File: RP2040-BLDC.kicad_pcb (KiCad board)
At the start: 4 copper layers, 40.2 x 35.8 mm, 33 parts, among them J1 Motor, J2 Conn_01x02, J3 USB_B_Micro, J4 Motor power, U2 AS5048A, U6 RP2040

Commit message: WIP
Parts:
- removed H1, H2, H3, H4: MountingHole, MountingHole:MountingHole_3.2mm_M3
- added C18: 4.7u, Capacitor_SMD:C_0805_2012Metric, F.Cu at (58.4, 45.0)
- added C19: 0.1u, Capacitor_SMD:C_0402_1005Metric, F.Cu at (54.8, 43.4)
- added C20: 0.1u, Capacitor_SMD:C_0402_1005Metric, F.Cu at (54.8, 45.4)
- added C21: 22u, Capacitor_SMD:CP_Elec_5x5.4, F.Cu at (80.6, 38.5)
- added C22: 22u, Capacitor_SMD:CP_Elec_5x5.4, F.Cu at (80.2, 45.0)
- added C23: 0.1u, Capacitor_SMD:C_0402_1005Metric, F.Cu at (61.8, 96.7)
- added C24: 0.1u, Capacitor_SMD:C_0402_1005Metric, F.Cu at (60.2, 98.9)
- added C25: 4.7u, Capacitor_SMD:C_0805_2012Metric, F.Cu at (69.5, 98.4)
- added C26: 0.1u, Capacitor_SMD:C_0402_1005Metric, F.Cu at (63.5, 102.0)
- added C27: 0.1u, Capacitor_SMD:C_0402_1005Metric, F.Cu at (62.1, 99.7)
- added C28: 22u, Capacitor_SMD:CP_Elec_5x5.4, F.Cu at (58.2, 104.2)
- added C29: 22u, Capacitor_SMD:CP_Elec_5x5.4, F.Cu at (80.0, 96.8)
- added C3: 0.1u, Capacitor_SMD:C_0402_1005Metric, F.Cu at (54.8, 39.5)
- added C5: 0.1u, Capacitor_SMD:C_0402_1005Metric, F.Cu at (54.8, 41.5)
- added D2: MBR1020VL, Diode_SMD:D_SOD-123F, F.Cu at (79.0, 59.1)
- added J5: AS5048A, Connector_JST:JST_SH_BM05B-SRSS-TB_1x05-1MP_P1.00mm_Vertical, F.Cu at (88.1, 51.3)
- added J6: M1, Connector_JST:JST_XH_S3B-XH-A_1x03_P2.50mm_Horizontal, F.Cu at (69.9, 45.0)
- added J7: M2, Connector_JST:JST_XH_S3B-XH-A_1x03_P2.50mm_Horizontal, F.Cu at (64.8, 106.4)
- added J8: AS5048A, Connector_JST:JST_SH_BM05B-SRSS-TB_1x05-1MP_P1.00mm_Vertical, F.Cu at (66.0, 91.8)
- added R6: 5.1k, Resistor_SMD:R_0402_1005Metric, F.Cu at (63.1, 52.1)
- added R7: 5.1k, Resistor_SMD:R_0402_1005Metric, F.Cu at (59.0, 94.2)
- J1: value Motor -> MPWR; footprint Connector_JST:JST_XH_B3B-XH-A_1x03_P2.50mm_Vertical -> Connector_PinHeader_2.54mm:PinHeader_1x02_P2.54mm_Vertical
- J4: value Motor power -> I2C5V; footprint Connector_JST:JST_XH_B2B-XH-A_1x02_P2.50mm_Vertical -> Connector_JST:JST_SH_BM04B-SRSS-TB_1x04-1MP_P1.00mm_Vertical
- U2: value AS5048A -> ~; footprint Package_SO:TSSOP-14_4.4x5mm_P0.65mm -> MyLibrary:WQFN-24_EP_2.93x2.93_Pitch0.4mm; moved to F.Cu
- moved J3 57.5 mm to (86.1, 74.6), turned to 90 degrees
- moved R2 54.6 mm to (80.2, 66.6), turned to 90 degrees
- moved C4 53.6 mm to (80.2, 69.0), turned to -90 degrees
- moved D1 51.9 mm to (81.4, 83.9), turned to 0 degrees
- moved U1 50.3 mm to (77.3, 67.3), turned to -90 degrees
- moved C17 49.2 mm to (77.8, 72.4), turned to 0 degrees
- moved C6 49.2 mm to (77.6, 71.4), turned to 0 degrees
- moved R1 48.9 mm to (75.3, 64.9), turned to -90 degrees
- moved C9 48.4 mm to (77.4, 73.5), turned to 0 degrees
- moved R4 47.4 mm to (76.8, 74.5), turned to 180 degrees
- moved R5 47.2 mm to (76.8, 75.5), turned to 180 degrees
- moved C8 46.9 mm to (76.7, 76.5), turned to 0 degrees
- moved C10 46.9 mm to (76.7, 77.5), turned to 0 degrees
- moved J2 45.8 mm to (72.9, 64.9), turned to -90 degrees
- moved C11 45.3 mm to (73.8, 68.1), turned to 90 degrees
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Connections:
- D1 pad 1: VCOM -> +5V
- J1 pad 1: /M1 -> GND
- J1 pad 2: /M2 -> +BATT
- J4 pad 1: GND -> /I2C0_SCL
- J4 pad 2: Vdrive -> /I2C0_SDA
- U2 pad 1: unconnected-(U2-~{CSn}-Pad1) -> /Driver sensor pair/DRV~{FAULT}
- U2 pad 10: unconnected-(U2-TEST-Pad10) -> /Driver sensor pair/MA
- U2 pad 11: unconnected-(U2-VDD5V-Pad11) -> /Driver sensor pair/MB
- U2 pad 12: unconnected-(U2-VDD3V-Pad12) -> /Driver sensor pair/MC
- U2 pad 2: unconnected-(U2-CLK-Pad2) -> Net-(U2-CSAREF)
- U2 pad 3: unconnected-(U2-MISO-Pad3) -> /Driver sensor pair/SOC
- U2 pad 4: unconnected-(U2-MOSI-Pad4) -> /Driver sensor pair/SOB
- U2 pad 5: unconnected-(U2-TEST-Pad5) -> /Driver sensor pair/SOA
- U2 pad 6: unconnected-(U2-TEST-Pad6) -> Net-(U2-CP)
- U2 pad 7: unconnected-(U2-TEST-Pad7) -> +5V
- U2 pad 8: unconnected-(U2-TEST-Pad8) -> +BATT
- U2 pad 9: unconnected-(U2-TEST-Pad9) -> GND
- U3 pad 1: unconnected-(U3-~{FAULT}-Pad1) -> /Driver sensor pair1/DRV~{FAULT}
- U3 pad 10: /M1 -> /Driver sensor pair1/MA
- U3 pad 11: /M2 -> /Driver sensor pair1/MB
- U3 pad 12: /M3 -> /Driver sensor pair1/MC
- U3 pad 17: unconnected-(U3-AVDD-Pad17) -> /Driver sensor pair1/3.3VOUT
- U3 pad 19: unconnected-(U3-PWM_SYNC-Pad19) -> /Driver sensor pair1/PWM_SYNC
- U3 pad 2: unconnected-(U3-CSAREF-Pad2) -> Net-(U3-CSAREF)
- U3 pad 20: /DRV_CSn -> /Driver sensor pair1/DRV~{CS}
- U3 pad 21: /SPI0_RX -> /Driver sensor pair1/SDO
- U3 pad 22: /SPI0_TX -> /Driver sensor pair1/SDI
- U3 pad 23: /SPI0_SCK -> /Driver sensor pair1/SPI_CLK
- U3 pad 24: unconnected-(U3-~{SLEEP}-Pad24) -> /Driver sensor pair1/~{SLEEP}
- U3 pad 25: (no net) -> GND
- U3 pad 3: unconnected-(U3-SOC-Pad3) -> /Driver sensor pair1/SOC
- U3 pad 4: unconnected-(U3-SOB-Pad4) -> /Driver sensor pair1/SOB
- U3 pad 5: unconnected-(U3-SOA-Pad5) -> /Driver sensor pair1/SOA
- U3 pad 6: unconnected-(U3-CP-Pad6) -> Net-(U3-CP)
- U3 pad 7: VCOM -> +5V
- U3 pad 8: Vdrive -> +BATT
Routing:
- net +5V: track 0.00 -> 36.9 mm, vias 0 -> 4
- net +3V3: track 19.9 -> 0.00 mm
- net /QSPI_SS: track 12.8 -> 0.00 mm
- net /USB_D+: track 10.5 -> 0.00 mm
- net /USB_D-: track 10.5 -> 0.00 mm
- net /Driver sensor pair1/SPI_CLK: track 0.00 -> 10.2 mm
- net /QSPI_SD1: track 9.04 -> 0.00 mm
- net /QSPI_SD2: track 7.64 -> 0.00 mm
- net +1V1: track 7.51 -> 0.00 mm
- net /QSPI_SD3: track 6.37 -> 0.00 mm
- net /QSPI_SCLK: track 5.75 -> 0.00 mm
- net /QSPI_SD0: track 5.13 -> 0.00 mm
- net /M1: track 4.74 -> 0.00 mm
- net /M3: track 4.23 -> 0.00 mm
- net Net-(U3-CP): track 0.00 -> 4.05 mm
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- added copper zone on F.Cu, net +5V
- added copper zone on F.Cu, net +BATT
- added copper zone on F.Cu, net /Driver sensor pair1/MA
- added copper zone on F.Cu, net /Driver sensor pair1/MB
- added copper zone on F.Cu, net /Driver sensor pair1/MC
- added copper zone on F.Cu, net GND
- added copper zone on In1.Cu, net GND
- added copper zone on In2.Cu, net GND
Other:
- board size 40.2 x 35.8 mm -> 41.4 x 81.2 mm

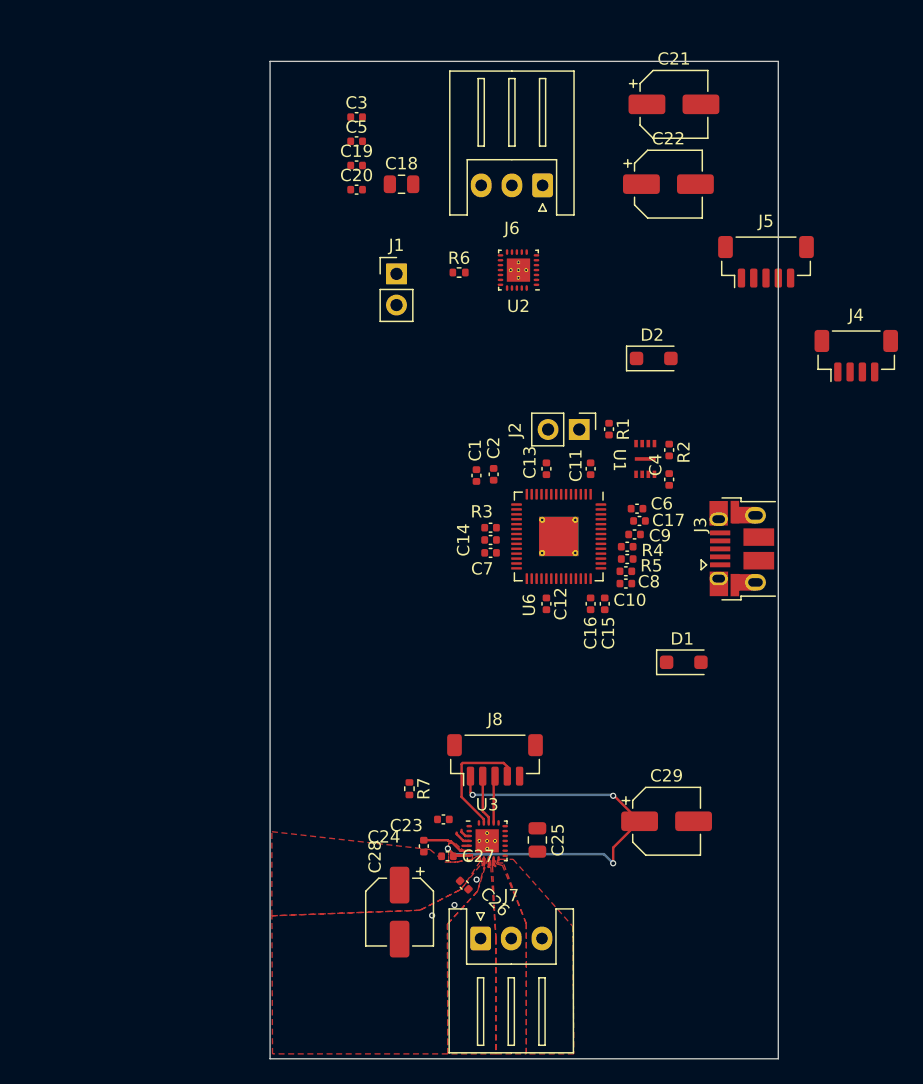
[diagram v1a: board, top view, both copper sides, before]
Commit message: First pass at routing board.
- Add INA219 current sensor and shunt
- Route motor traces.
- Still need to fix a few footprints.
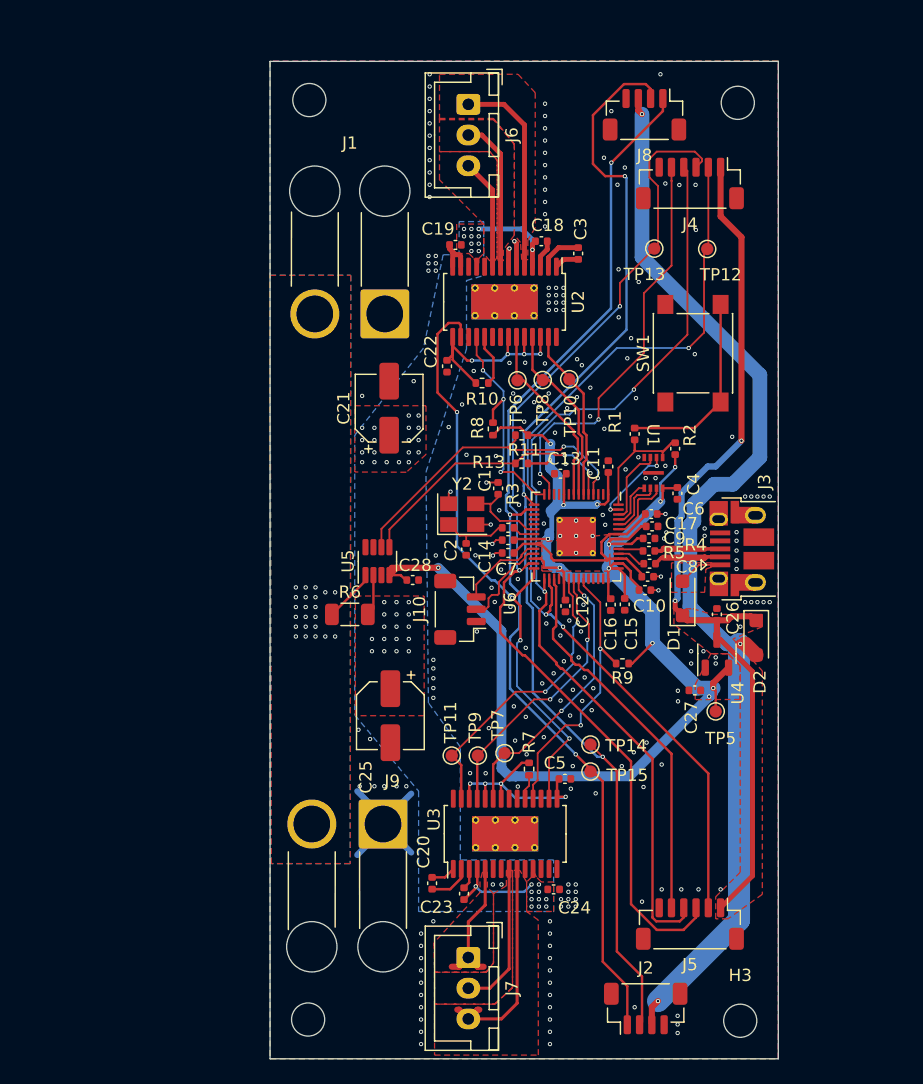
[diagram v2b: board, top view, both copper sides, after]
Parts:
- removed C29: 22u, Capacitor_SMD:CP_Elec_5x5.4
- added H1: MountingHole, MountingHole:MountingHole_2.7mm_M2.5, F.Cu at (50.9, 38.1)
- added H2: MountingHole, MountingHole:MountingHole_2.7mm_M2.5, F.Cu at (85.8, 38.3)
- added H3: MountingHole, MountingHole:MountingHole_2.7mm_M2.5, F.Cu at (86.0, 113.1)
- added H4: MountingHole, MountingHole:MountingHole_2.7mm_M2.5, F.Cu at (50.8, 113.0)
- added J10: DBG, Connector_JST:JST_SH_BM03B-SRSS-TB_1x03-1MP_P1.00mm_Vertical, F.Cu at (63.2, 79.6)
- added J9: MPWR, MyLibrary:SolderWire-2.5sqmm_1x02_P7.2mm_D2.4mm_OD3.6mm_ShortRelief, F.Cu at (56.9, 97.1)
- added R10: 10k, Resistor_SMD:R_0402_1005Metric, F.Cu at (65.0, 61.1)
- added R11: 2k, Resistor_SMD:R_0402_1005Metric, F.Cu at (68.2, 65.4)
- added R13: 2k, Resistor_SMD:R_0402_1005Metric, F.Cu at (68.2, 67.7)
- added R8: 10k, Resistor_SMD:R_0402_1005Metric, F.Cu at (65.9, 64.9)
- added R9: 10k, Resistor_SMD:R_0402_1005Metric, F.Cu at (76.4, 84.0)
- added SW1: Flash, Button_Switch_SMD:SW_Push_1P1T_NO_6x6mm_H9.5mm, F.Cu at (82.2, 58.7)
- added TP10: TestPoint_Small, TestPoint:TestPoint_Pad_D1.0mm, F.Cu at (72.1, 60.8)
- added TP11: TestPoint_Small, TestPoint:TestPoint_Pad_D1.0mm, F.Cu at (62.5, 91.5)
- added TP12: TestPoint_Small, TestPoint:TestPoint_Pad_D1.0mm, F.Cu at (83.3, 50.2)
- added TP13: TestPoint_Small, TestPoint:TestPoint_Pad_D1.0mm, F.Cu at (79.0, 50.2)
- added TP14: TestPoint_Small, TestPoint:TestPoint_Pad_D1.0mm, F.Cu at (73.8, 90.6)
- added TP15: TestPoint_Small, TestPoint:TestPoint_Pad_D1.0mm, F.Cu at (73.8, 92.8)
- added TP5: TestPoint_Small, TestPoint:TestPoint_Pad_D1.0mm, F.Cu at (84.0, 87.9)
- added TP6: TestPoint_Small, TestPoint:TestPoint_Pad_D1.0mm, F.Cu at (67.8, 60.9)
- added TP7: TestPoint_Small, TestPoint:TestPoint_Pad_D1.0mm, F.Cu at (66.8, 91.3)
- added TP8: TestPoint_Small, TestPoint:TestPoint_Pad_D1.0mm, F.Cu at (69.9, 60.9)
- added TP9: TestPoint_Small, TestPoint:TestPoint_Pad_D1.0mm, F.Cu at (64.6, 91.5)
- added U4: XC6206PxxxMR, Package_TO_SOT_SMD:SOT-23-3, F.Cu at (84.1, 83.2)
- added U5: INA219AxDCN, Package_TO_SOT_SMD:SOT-23-8, F.Cu at (56.4, 75.7)
- added Y2: 12MHz X322512MSB4SI, Crystal:Crystal_SMD_3225-4Pin_3.2x2.5mm, F.Cu at (63.4, 71.8)
- C18: value 4.7u -> 0.1u; footprint Capacitor_SMD:C_0805_2012Metric -> Capacitor_SMD:C_0402_1005Metric
- C20, C3: value 0.1u -> 0.01u
- C21: value 22u -> 100u
- C22: value 22u -> 0.47u; footprint Capacitor_SMD:CP_Elec_5x5.4 -> Capacitor_SMD:C_0402_1005Metric
- C25: value 4.7u -> 100u; footprint Capacitor_SMD:C_0805_2012Metric -> Capacitor_SMD:CP_Elec_5x5.4
- C26, C27: value 0.1u -> 1u
- C28: value 22u -> C_Small; footprint Capacitor_SMD:CP_Elec_5x5.4 -> Capacitor_SMD:C_0402_1005Metric
- C5: value 0.1u -> 0.47u
- J1: footprint Connector_PinHeader_2.54mm:PinHeader_1x02_P2.54mm_Vertical -> MyLibrary:SolderWire-2.5sqmm_1x02_P7.2mm_D2.4mm_OD3.6mm_ShortRelief_Flipped
- J2: value Conn_01x02 -> Conn_01x04_MountingPin; footprint Connector_PinHeader_2.54mm:PinHeader_1x02_P2.54mm_Vertical -> Connector_JST:JST_SH_BM04B-SRSS-TB_1x04-1MP_P1.00mm_Vertical
- J4: value I2C5V -> Conn_01x06_MountingPin; footprint Connector_JST:JST_SH_BM04B-SRSS-TB_1x04-1MP_P1.00mm_Vertical -> Connector_JST:JST_SH_BM06B-SRSS-TB_1x06-1MP_P1.00mm_Vertical
- J5: value AS5048A -> Conn_01x06_MountingPin; footprint Connector_JST:JST_SH_BM05B-SRSS-TB_1x05-1MP_P1.00mm_Vertical -> Connector_JST:JST_SH_BM06B-SRSS-TB_1x06-1MP_P1.00mm_Vertical
- J6, J7: footprint Connector_JST:JST_XH_S3B-XH-A_1x03_P2.50mm_Horizontal -> Connector_JST:JST_XH_B3B-XH-A_1x03_P2.50mm_Vertical
- J8: value AS5048A -> Conn_01x04_MountingPin; footprint Connector_JST:JST_SH_BM05B-SRSS-TB_1x05-1MP_P1.00mm_Vertical -> Connector_JST:JST_SH_BM04B-SRSS-TB_1x04-1MP_P1.00mm_Vertical
- R6: value 5.1k -> 0.01; footprint Resistor_SMD:R_0402_1005Metric -> Resistor_SMD:R_1206_3216Metric
- R7: value 5.1k -> 10k
- U2, U3: value ~ -> DRV8313; footprint MyLibrary:WQFN-24_EP_2.93x2.93_Pitch0.4mm -> Package_SO:HTSSOP-28-1EP_4.4x9.7mm_P0.65mm_EP2.85x5.4mm_ThermalVias
- moved C20 56.8 mm to (60.9, 101.9), turned to -90 degrees
- moved C5 54.6 mm to (71.7, 93.4)
- moved J5 54.3 mm to (81.9, 105.2), turned to 180 degrees
- moved J8 53.9 mm to (78.2, 39.3), turned to 180 degrees
- moved J2 47.5 mm to (78.3, 112.1), turned to 0 degrees
- moved C21 33.9 mm to (57.4, 63.2), turned to 90 degrees
- moved C26 30.2 mm to (84.1, 80.0), turned to 90 degrees
- moved R6 29.2 mm to (54.2, 80.0)
- moved C28 27.1 mm to (59.3, 77.2), turned to 0 degrees
- moved C27 24.3 mm to (82.3, 86.2)
- moved D2 24.2 mm to (87.3, 81.9), turned to -90 degrees
- moved C22 23.4 mm to (62.1, 59.8), turned to -90 degrees
- moved C3 21.2 mm to (72.8, 50.6), turned to 90 degrees
- moved J4 19.5 mm to (81.9, 44.9), turned to 180 degrees
- moved C25 15.7 mm to (57.5, 88.2)
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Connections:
- C18 pad 1: +3.3V -> +BATT
- C18 pad 2: GND -> Net-(U2-VCP)
- C20 pad 1: +5V -> Net-(U3-CPL)
- C20 pad 2: GND -> Net-(U3-CPH)
- C22 pad 1: +5V -> /Driver sensor pair/DRV3.3VOUT
- C23 pad 1: Net-(U3-CSAREF) -> +BATT
- C23 pad 2: GND -> Net-(U3-VCP)
- C24 pad 2: Net-(U3-CP) -> GND
- C25 pad 1: /Driver sensor pair1/3.3VOUT -> +BATT
- C26 pad 1: +BATT -> +5V
- C27 pad 1: +5V -> +3V3
- C28 pad 1: +BATT -> +3V3
- C3 pad 1: Net-(U2-CSAREF) -> Net-(U2-CPL)
- C3 pad 2: GND -> Net-(U2-CPH)
- C5 pad 1: +BATT -> /Driver sensor pair1/DRV3.3VOUT
- C5 pad 2: Net-(U2-CP) -> GND
- J1 pad 2: +BATT -> Net-(J1-Pin_2)
- J2 pad 1: /~{USB_BOOT} -> /I2C0_SCL
- J2 pad 2: GND -> /I2C0_SDA
- J4 pad 1: /I2C0_SCL -> +5V
- J4 pad 2: /I2C0_SDA -> /SPI0_TX
- J4 pad 3: Net-(D2-A) -> /SPI0_RX
- J4 pad 4: GND -> /SPI0_SCK
- J4 pad MP: (no net) -> GND
- J5 pad 2: /Driver sensor pair/SDI -> /SPI0_TX
- J5 pad 3: /Driver sensor pair/SDO -> /SPI0_RX
- J5 pad 4: /Driver sensor pair/SPI_CLK -> /SPI0_SCK
- J5 pad 5: /Driver sensor pair/SEN~{CS} -> /SEN2CS
- J5 pad MP: (no net) -> GND
- J8 pad 1: +5V -> /I2C0_SCL
- J8 pad 2: /Driver sensor pair1/SDI -> /I2C0_SDA
- J8 pad 3: /Driver sensor pair1/SDO -> Net-(D2-A)
- J8 pad 4: /Driver sensor pair1/SPI_CLK -> GND
- J8 pad MP: (no net) -> GND
- R6 pad 1: +3.3V -> Net-(J1-Pin_2)
- R6 pad 2: /Driver sensor pair/DRV~{FAULT} -> +BATT
- R7 pad 1: /Driver sensor pair1/3.3VOUT -> Net-(U3-~{COMPO})
- R7 pad 2: /Driver sensor pair1/DRV~{FAULT} -> /Driver sensor pair1/DRV3.3VOUT
- U2 pad 1: /Driver sensor pair/DRV~{FAULT} -> Net-(U2-CPL)
- U2 pad 10: /Driver sensor pair/MA -> GND
- U2 pad 11: /Driver sensor pair/MB -> +BATT
- U2 pad 12: /Driver sensor pair/MC -> GND
- U2 pad 13: unconnected-(U2-NC-Pad13) -> GND
- U2 pad 14: unconnected-(U2-AD1-Pad14) -> GND
- U2 pad 15: unconnected-(U2-AD0-Pad15) -> /Driver sensor pair/DRV3.3VOUT
- U2 pad 16: GND -> /DRV~{RESET}
- U2 pad 17: +3.3V -> /Driver sensor pair/~{SLEEP}
- U2 pad 18: unconnected-(U2-NC-Pad18) -> /DRV1FAULT
- U2 pad 19: /Driver sensor pair/PWM_SYNC -> Net-(U2-~{COMPO})
- U2 pad 2: Net-(U2-CSAREF) -> Net-(U2-CPH)
- U2 pad 20: /Driver sensor pair/DRV~{CS} -> GND
- U2 pad 21: /Driver sensor pair/SDO -> unconnected-(U2-NC-Pad21)
- U2 pad 22: /Driver sensor pair/SDI -> /Driver sensor pair/DRV3.3VOUT
- U2 pad 23: /Driver sensor pair/SPI_CLK -> /DRV1IN3
- U2 pad 24: /Driver sensor pair/~{SLEEP} -> /Driver sensor pair/DRV3.3VOUT
- U2 pad 25: GND -> /DRV1IN2
- U2 pad 3: /Driver sensor pair/SOC -> Net-(U2-VCP)
- U2 pad 4: /Driver sensor pair/SOB -> +BATT
- U2 pad 5: /Driver sensor pair/SOA -> /Driver sensor pair/MA
- U2 pad 6: Net-(U2-CP) -> GND
- U2 pad 7: +5V -> GND
- U2 pad 8: +BATT -> /Driver sensor pair/MB
- U2 pad 9: GND -> /Driver sensor pair/MC
- U3 pad 1: /Driver sensor pair1/DRV~{FAULT} -> Net-(U3-CPL)
- U3 pad 10: /Driver sensor pair1/MA -> GND
- U3 pad 11: /Driver sensor pair1/MB -> +BATT
- U3 pad 12: /Driver sensor pair1/MC -> GND
- U3 pad 13: unconnected-(U3-NC-Pad13) -> GND
- U3 pad 14: unconnected-(U3-AD1-Pad14) -> GND
- U3 pad 15: unconnected-(U3-AD0-Pad15) -> /Driver sensor pair1/DRV3.3VOUT
- U3 pad 16: GND -> /DRV~{RESET}
- U3 pad 17: /Driver sensor pair1/3.3VOUT -> /Driver sensor pair1/~{SLEEP}
- U3 pad 18: unconnected-(U3-NC-Pad18) -> /DRV2FAULT
- U3 pad 19: /Driver sensor pair1/PWM_SYNC -> Net-(U3-~{COMPO})
- U3 pad 2: Net-(U3-CSAREF) -> Net-(U3-CPH)
- U3 pad 20: /Driver sensor pair1/DRV~{CS} -> GND
- U3 pad 21: /Driver sensor pair1/SDO -> unconnected-(U3-NC-Pad21)
- U3 pad 22: /Driver sensor pair1/SDI -> /Driver sensor pair1/DRV3.3VOUT
- U3 pad 23: /Driver sensor pair1/SPI_CLK -> /DRV2IN3
- U3 pad 24: /Driver sensor pair1/~{SLEEP} -> /Driver sensor pair1/DRV3.3VOUT
- U3 pad 25: GND -> /DRV2IN2
- U3 pad 3: /Driver sensor pair1/SOC -> Net-(U3-VCP)
- U3 pad 4: /Driver sensor pair1/SOB -> +BATT
- U3 pad 5: /Driver sensor pair1/SOA -> /Driver sensor pair1/MA
- U3 pad 6: Net-(U3-CP) -> GND
- U3 pad 7: +5V -> GND
- U3 pad 8: +BATT -> /Driver sensor pair1/MB
- U3 pad 9: GND -> /Driver sensor pair1/MC
- U6 pad 11: /GPIO8 -> unconnected-(U6-GPIO8-Pad11)
- U6 pad 12: /GPIO9 -> unconnected-(U6-GPIO9-Pad12)
- U6 pad 13: /GPIO10 -> /SEN1CS
- U6 pad 14: /GPIO11 -> /DRV1FAULT
- U6 pad 15: /GPIO12 -> /I2C0_SDA
- U6 pad 16: /GPIO13 -> /I2C0_SCL
- U6 pad 17: /GPIO14 -> unconnected-(U6-GPIO14-Pad17)
- U6 pad 18: /GPIO15 -> unconnected-(U6-GPIO15-Pad18)
- U6 pad 2: /GPIO0 -> unconnected-(U6-GPIO0-Pad2)
- U6 pad 26: /RUN -> +3V3
- U6 pad 28: /DRV_CSn -> /DRV~{RESET}
- U6 pad 3: /GPIO1 -> unconnected-(U6-GPIO1-Pad3)
- U6 pad 31: /GPIO20 -> /SEN2CS
- U6 pad 32: /GPIO21 -> unconnected-(U6-GPIO21-Pad32)
- U6 pad 34: /GPIO22 -> /DRV2IN1
- U6 pad 35: /GPIO23 -> /DRV2IN2
- U6 pad 36: /GPIO24 -> /DRV2IN3
- U6 pad 37: /GPIO25 -> /DRV2FAULT
- U6 pad 4: /GPIO2 -> /I2C1SDA
- U6 pad 5: /GPIO3 -> /I2C1SCL
- U6 pad 6: /GPIO4 -> /DRV1IN1
- U6 pad 7: /GPIO5 -> /DRV1IN2
- U6 pad 8: /GPIO6 -> /DRV1IN3
- U6 pad 9: /GPIO7 -> unconnected-(U6-GPIO7-Pad9)
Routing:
- net +3V3: track 0.00 -> 141.7 mm, vias 0 -> 14
- net /I2C0_SDA: track 0.00 -> 93.7 mm, vias 0 -> 3
- net Net-(D2-A): track 0.00 -> 89.8 mm, vias 0 -> 3
- net /I2C0_SCL: track 0.00 -> 88.0 mm, vias 0 -> 3
- net /SPI0_RX: track 0.00 -> 86.1 mm, vias 0 -> 2
- net /SPI0_TX: track 0.00 -> 78.9 mm, vias 0 -> 3
- net /SPI0_SCK: track 0.00 -> 78.2 mm, vias 0 -> 2
- net /DRV~{RESET}: track 0.00 -> 50.0 mm, vias 0 -> 4
- net +5V: track 36.9 -> 72.1 mm, vias 4 -> 2
- net /SEN1CS: track 0.00 -> 33.3 mm, vias 0 -> 2
- net /SEN2CS: track 0.00 -> 31.3 mm
- net /I2C1SDA: track 0.00 -> 26.2 mm, vias 0 -> 2
- net GND: track 0.56 -> 26.7 mm, vias 3 -> 232
- net /DRV2IN1: track 0.00 -> 24.3 mm, vias 0 -> 2
- net /DRV2FAULT: track 0.00 -> 23.3 mm, vias 0 -> 2
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- added copper zone on F.Cu, net +1V1
- added copper zone on F.Cu, net +3V3
- added copper zone on B.Cu, net +BATT
- added copper zone on F.Cu, net /Driver sensor pair/MA
- added copper zone on F.Cu, net /Driver sensor pair/MB
- added copper zone on F.Cu, net /Driver sensor pair/MC
- added copper zone on B.Cu, net GND
- added copper zone on B.Cu, net Net-(J1-Pin_2)
- added copper zone on F.Cu, net Net-(J1-Pin_2)
- added copper zone on F.Cu, net VBUS

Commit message: Make vias bigger
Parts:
- moved C11 0.08 mm to (75.3, 68.0)
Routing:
- net +3V3: track 141.7 -> 128.7 mm
- net /SPI0_RX: track 86.1 -> 87.8 mm
- net /Driver sensor pair/MA: track 16.8 -> 15.1 mm
- net GND: track 26.7 -> 28.3 mm, vias 232 -> 246
- net /I2C1SDA: track 26.2 -> 27.8 mm
- net /DRV~{RESET}: track 50.0 -> 51.2 mm
- net /QSPI_SD1: track 6.82 -> 7.52 mm
- net /SEN1CS: track 33.3 -> 34.0 mm
- net /DRV2IN3: track 22.5 -> 23.2 mm
- net Net-(J1-Pin_2): vias 22 -> 27
- added copper zone on B.Cu, net +3V3
